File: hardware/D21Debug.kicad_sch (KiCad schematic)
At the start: 61 parts, among them J1 Micro USB, J2 Conn_01x04_Male, J3 Conn_01x04_Male, SW1 SW_Push, SW2 SW_Push, SW3 SW_Push, SW4 SW_Push, SW5 SW_Push, U1 ATSAMD21E15L-A, U2 MIC5365-3.3YC5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

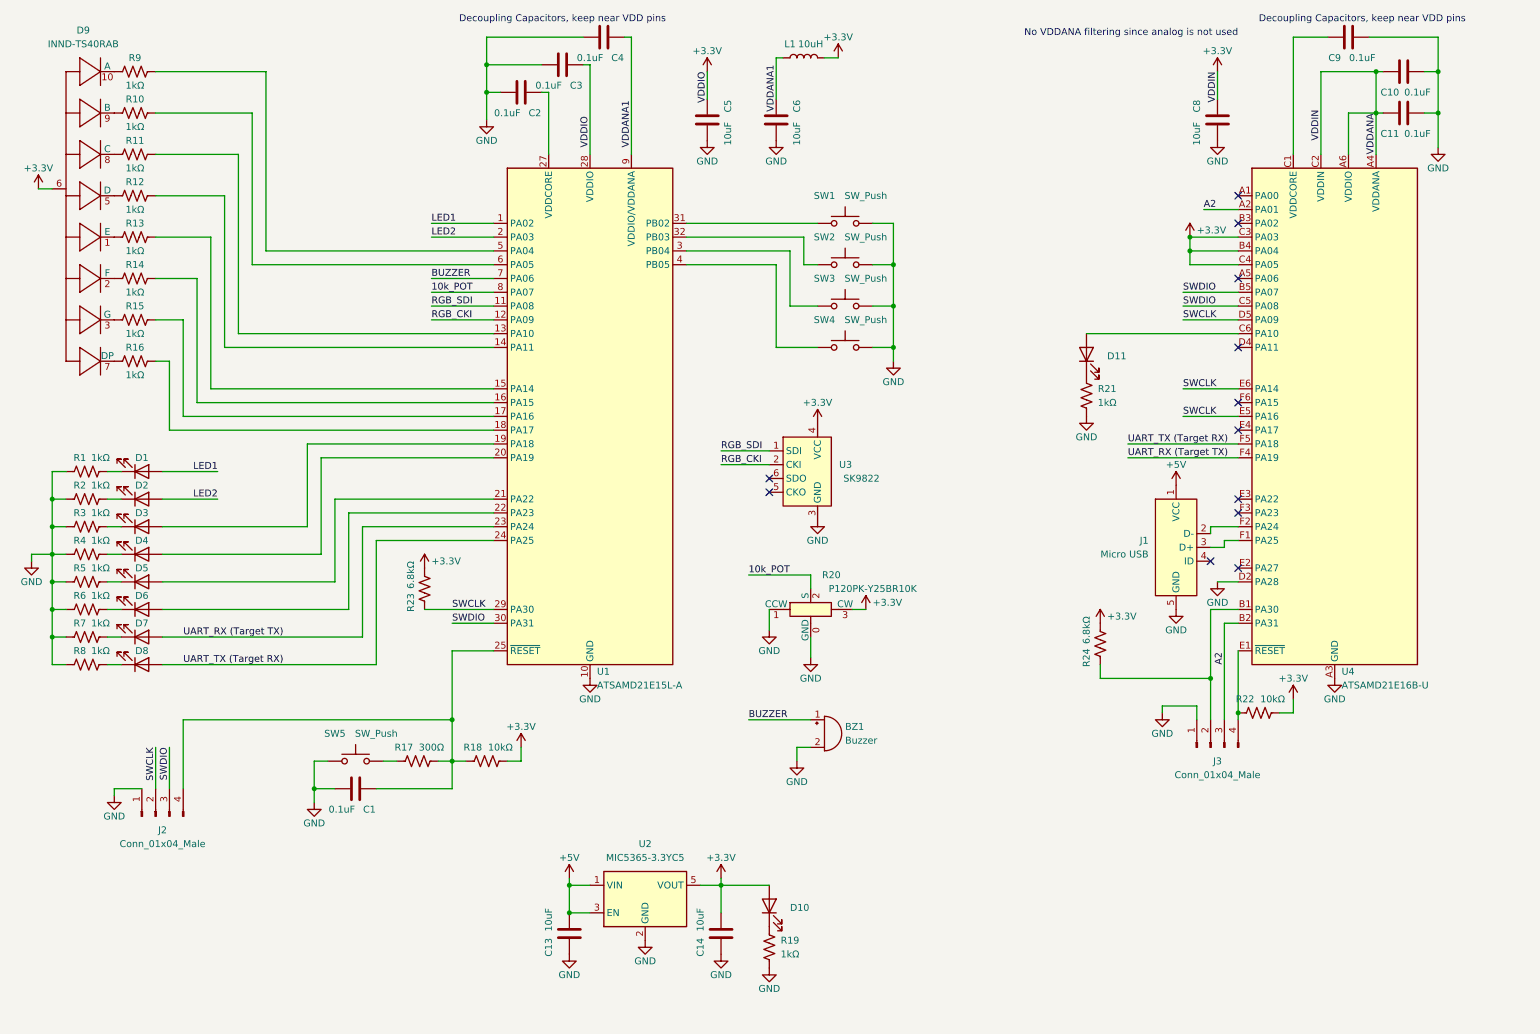
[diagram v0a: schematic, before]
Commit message: Cleaned up schematic and BOM
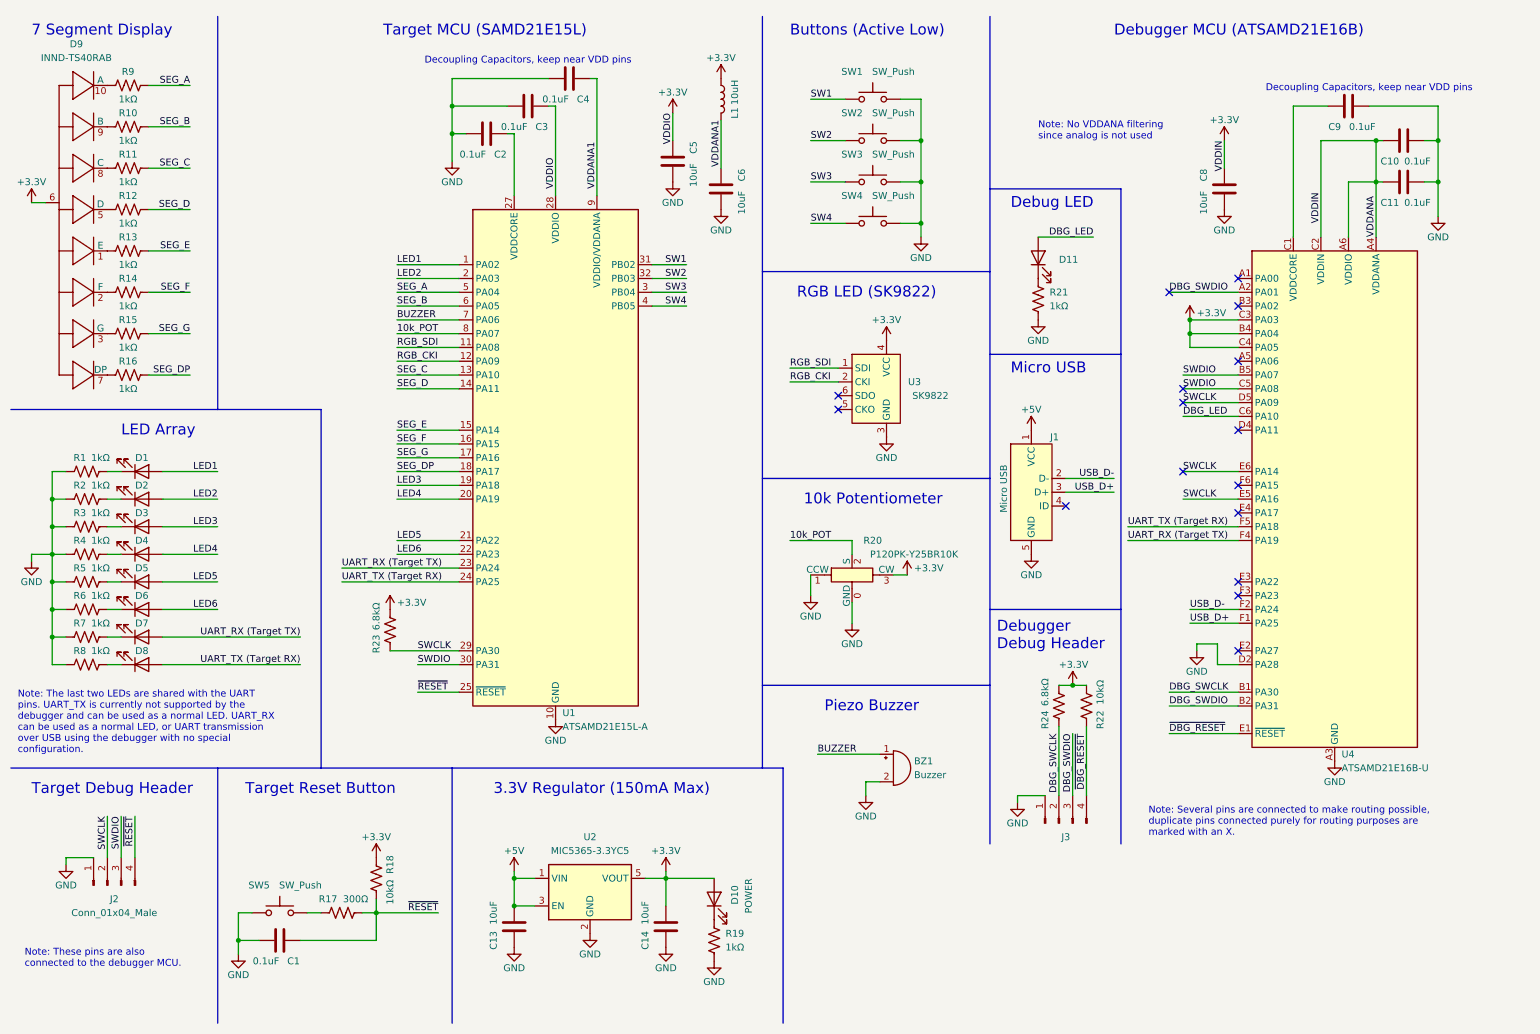
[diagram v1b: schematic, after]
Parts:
- D10: value (none) -> POWER
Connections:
- net +3V3: now also R18.1, R22.1; no longer R18.2, R22.2
- net USB_D-: now reaches J1.2 (D-), U4.F2 (PA24)
- net USB_D+: now reaches J1.3 (D+), U4.F1 (PA25)
- net SEG_C: now reaches R11.2, U1.13 (PA10)
- net SEG_D: now reaches R12.2, U1.14 (PA11)
- net SEG_E: now reaches R13.2, U1.15 (PA14)
- net SEG_F: now reaches R14.2, U1.16 (PA15)
- net SEG_G: now reaches R15.2, U1.17 (PA16)
- net SEG_DP: now reaches R16.2, U1.18 (PA17)
- net LED3: now reaches D3.2 (A), U1.19 (PA18)
- net LED4: now reaches D4.2 (A), U1.20 (PA19)
- net LED5: now reaches D5.2 (A), U1.21 (PA22)
- net LED6: now reaches D6.2 (A), U1.22 (PA23)
- net ~{RESET}: now reaches C1.1, J2.4 (Pin_4), R17.2, U1.25 (~{RESET})
- net ~{RESET}: now also R18.2; no longer R18.1
- net SW3: now reaches SW3.1, U1.3 (PB04)
- net SW1: now reaches SW1.1, U1.31 (PB02)
- net SW2: now reaches SW2.1, U1.32 (PB03)
- net SW4: now reaches SW4.1, U1.4 (PB05)
- net SEG_A: now reaches R9.2, U1.5 (PA04)
- net SEG_B: now reaches R10.2, U1.6 (PA05)
- net DBG_SWCLK: now reaches J3.2 (Pin_2), R24.1, U4.B1 (PA30)
- net ~{DBG_RESET}: now reaches J3.4 (Pin_4), U4.E1 (~{RESET})
- net ~{DBG_RESET}: now also R22.2; no longer R22.1
- net DBG_LED: now reaches D11.2 (A), U4.C6 (PA10)
- net A2 renamed DBG_SWDIO
- no-connect marks 12 -> 16
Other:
- note added: "10k Potentiometer"
- note added: "3.3V Regulator (150mA Max)"
- note added: "7 Segment Display"
- note added: "Buttons (Active Low)"
- note added: "Debug LED"
- note added: "Debugger Debug Header"
- note added: "Debugger MCU (ATSAMD21E16B)"
- note added: "LED Array"
- note added: "Micro USB"
- note added: "Note: No VDDANA filtering since analog is not used"
- note added: "Note: Several pins are connected to make routing possible, duplicate pins connected purely for routing purposes are marked with an X."
- note added: "Note: The last two LEDs are shared with the UART pins. UART_TX is currently not supported by the debugger and can be used as a normal LED. UART_RX can be used as a normal LED, or UART transmission over USB using the debugger with no special configuration."
- note added: "Note: These pins are also connected to the debugger MCU."
- note added: "Piezo Buzzer"
- note added: "RGB LED (SK9822)"
- note added: "Target Debug Header"
- note added: "Target MCU (SAMD21E15L)"
- note added: "Target Reset Button"
- note removed: "No VDDANA filtering since analog is not used"
- company: (none) -> Gregory Ling
- title: (none) -> SAM D21 Playground
- moved on the sheet: BZ1, C1, C10, C11, C13, C14, C2, C3, C4, C5, C6, C8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

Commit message: Fix reset line in schematic
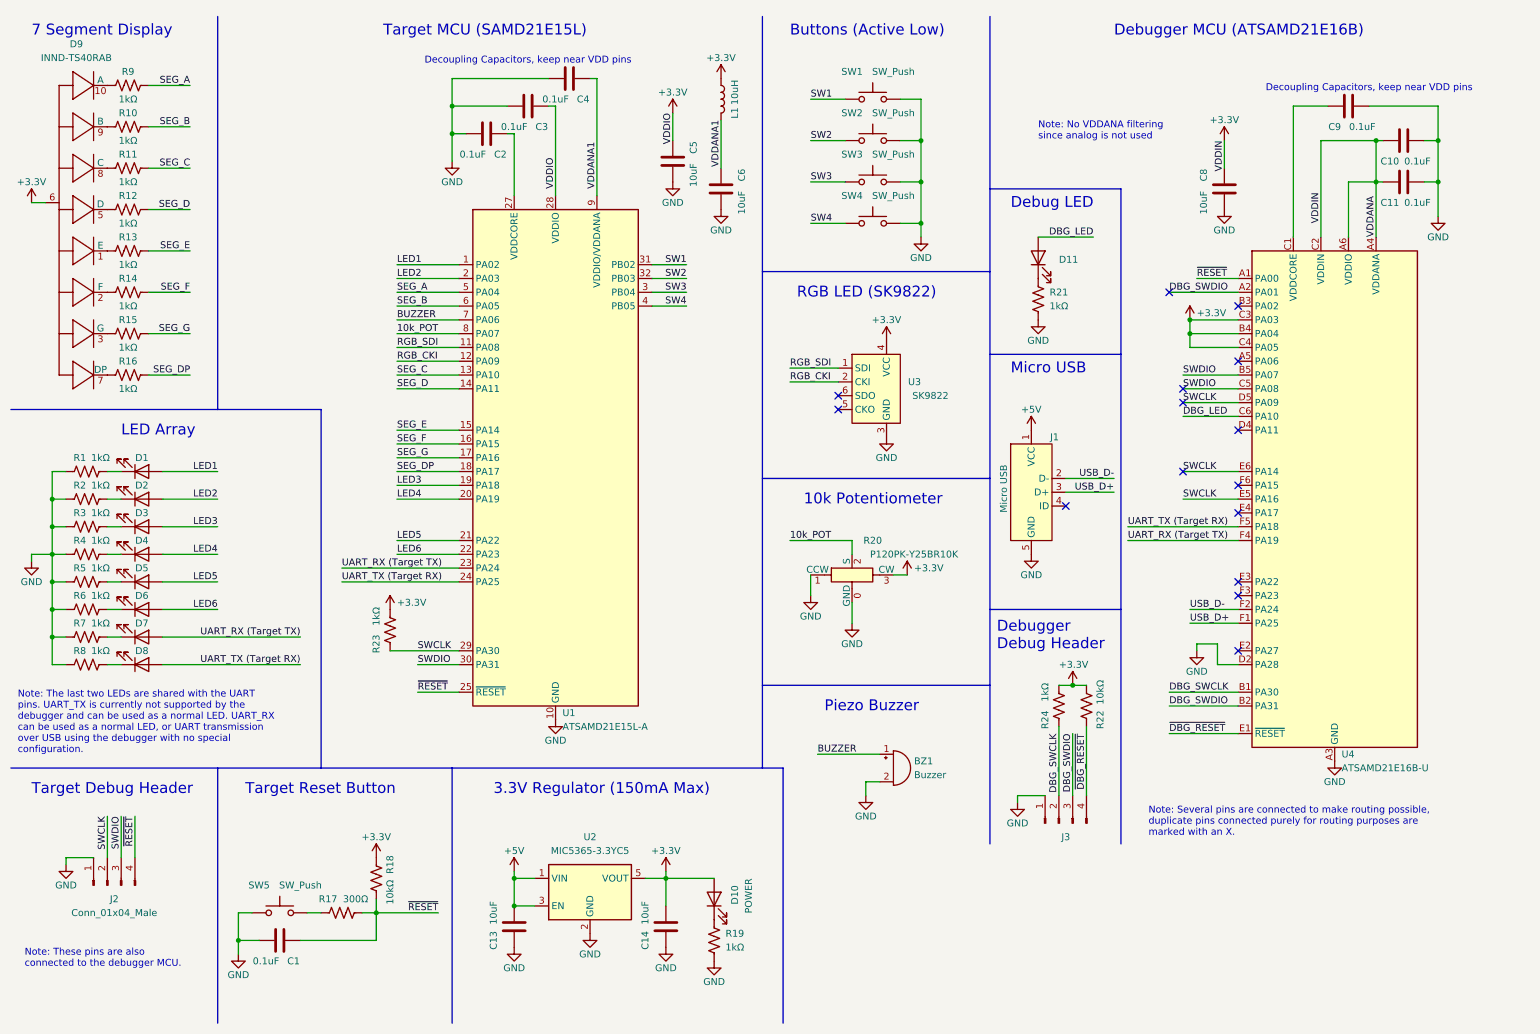
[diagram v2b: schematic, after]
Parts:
- R23, R24: value 6.8kΩ -> 1kΩ
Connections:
- net ~{RESET}: now also U4.A1 (PA00)
- no-connect marks 16 -> 15
